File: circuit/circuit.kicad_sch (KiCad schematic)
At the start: 3 parts, among them J1 USB_B_Mini, U1 ESP-C3-WROOM-02, U2 nRF52820-QDAA

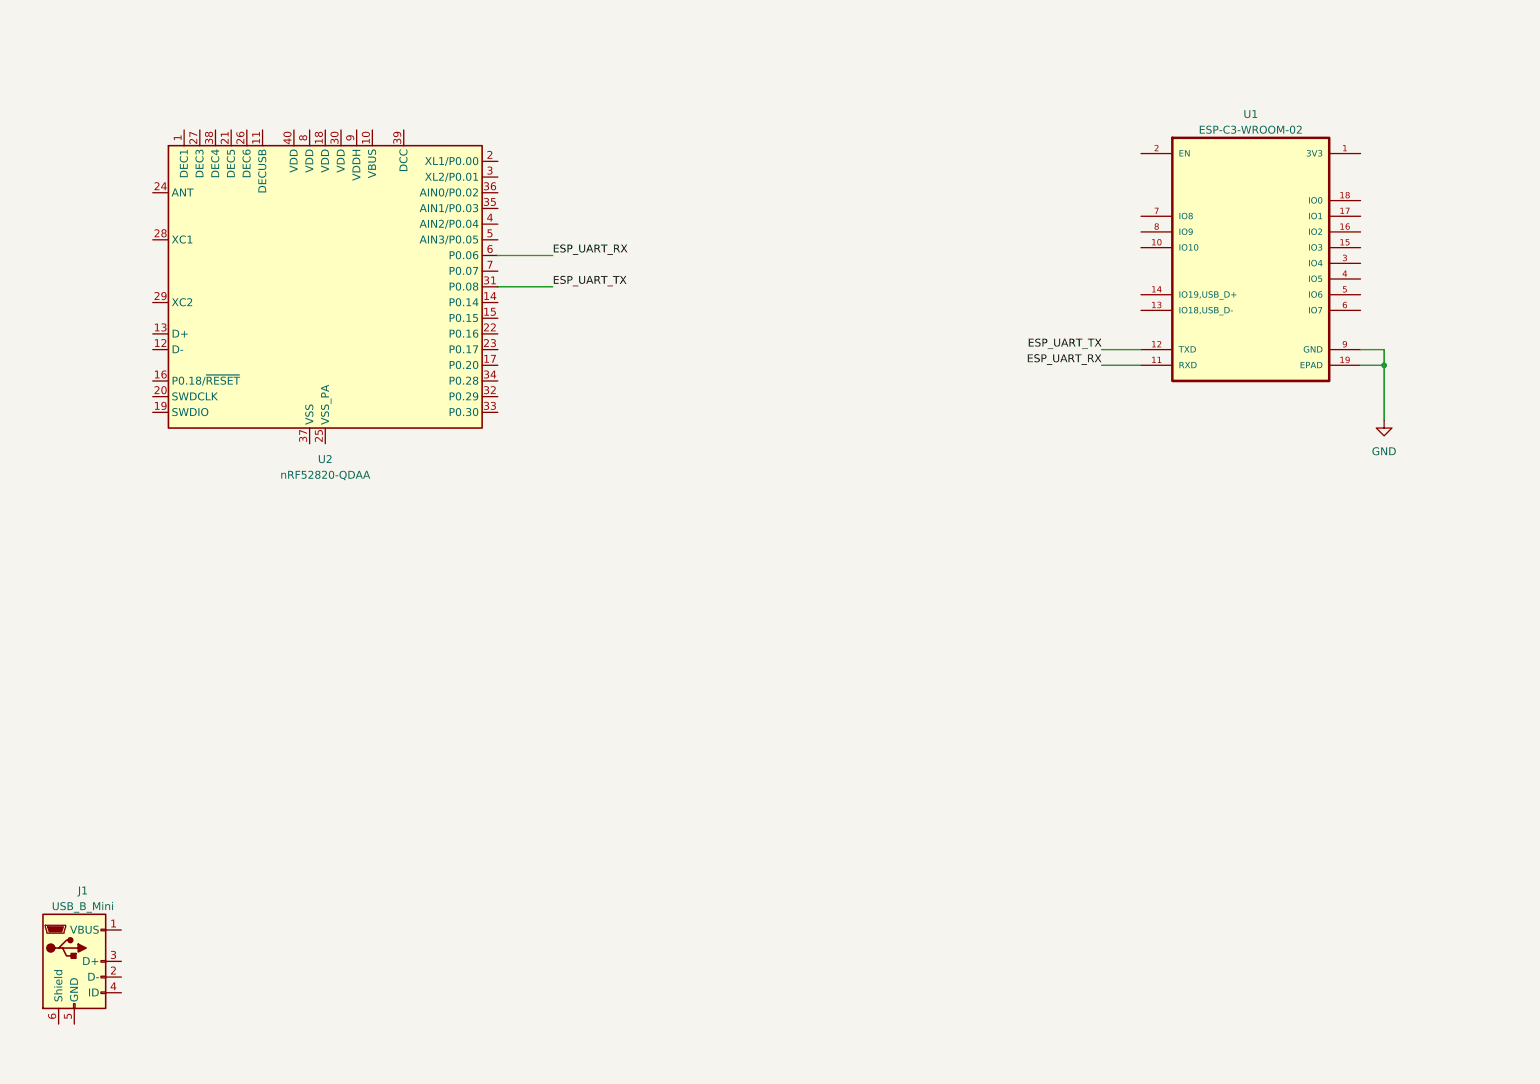
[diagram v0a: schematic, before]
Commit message: change(mdbt50): use module for 802.15.4
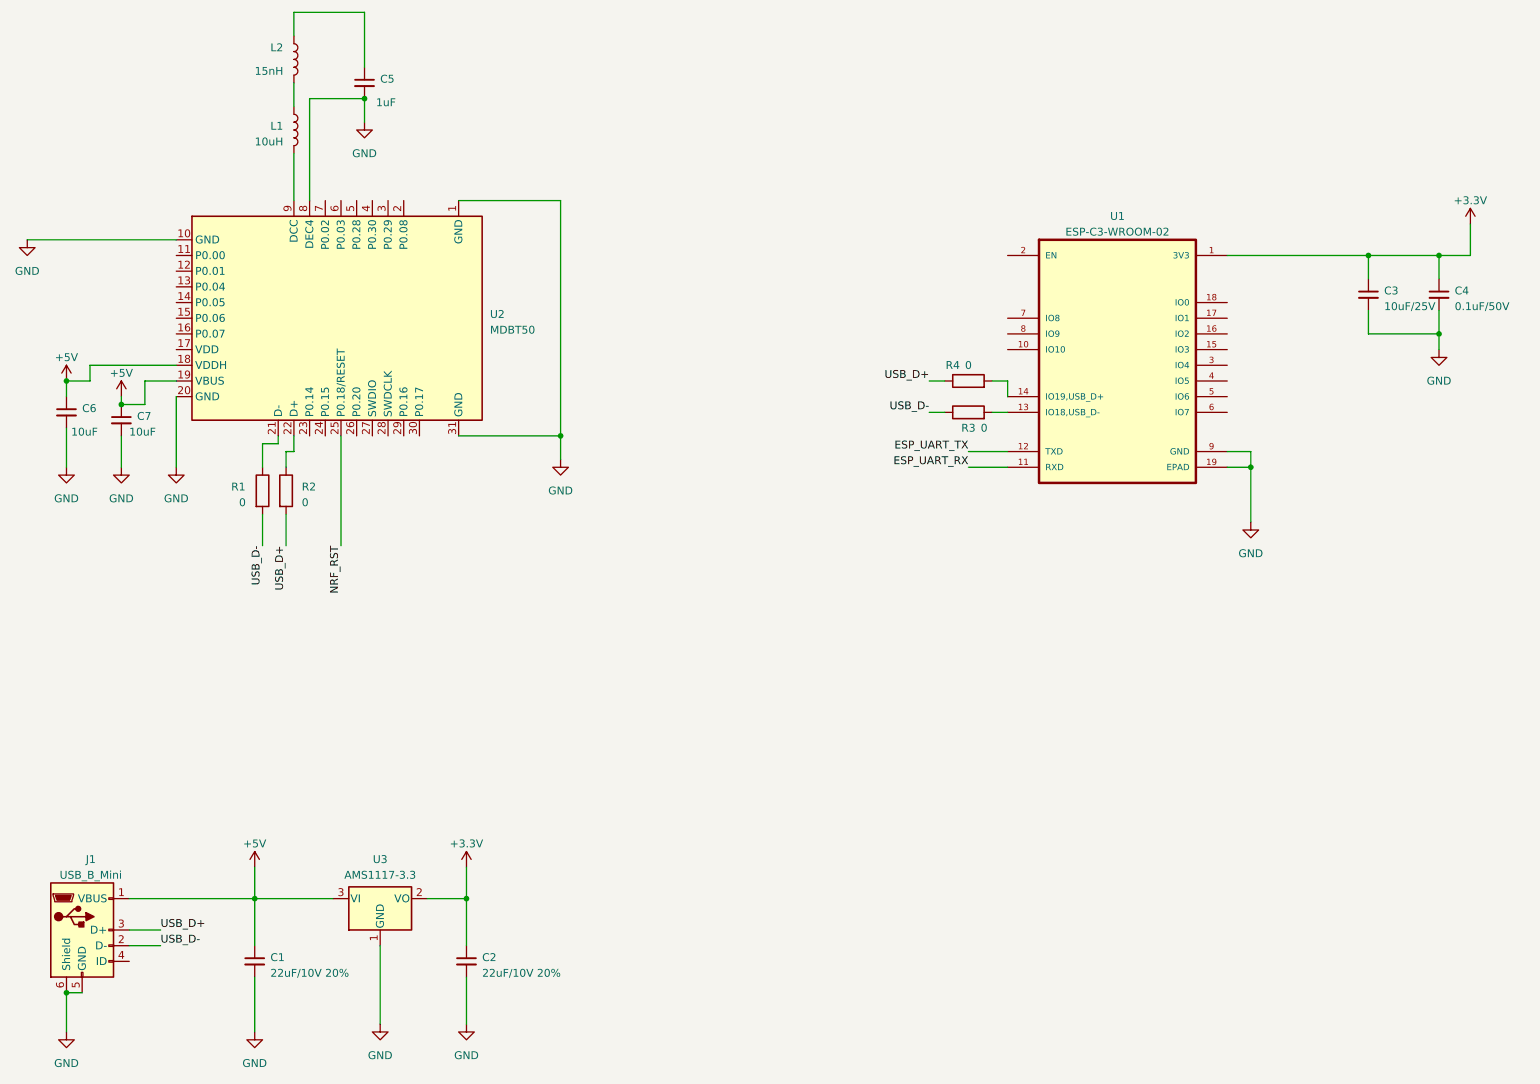
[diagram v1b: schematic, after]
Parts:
- removed U2: nRF52820-QDAA, Package_DFN_QFN:QFN-40-1EP_5x5mm_P0.4mm_EP3.6x3.6mm, symbol MCU_Nordic:nRF52820-QDxx
- added C1, C2: 22uF/10V 20%, Capacitor_SMD:C_0402_1005Metric, symbol Device:C_Small
- added C3: 10uF/25V, Capacitor_SMD:C_0402_1005Metric, symbol Device:C_Small
- added C4: 0.1uF/50V, Capacitor_SMD:C_0402_1005Metric, symbol Device:C_Small
- added C5: 1uF, Capacitor_SMD:C_0402_1005Metric, symbol Device:C_Small
- added C6, C7: 10uF, Capacitor_SMD:C_0402_1005Metric, symbol Device:C_Small
- added L1: 10uH, Inductor_SMD:L_0603_1608Metric, symbol Device:L
- added L2: 15nH, Inductor_SMD:L_0603_1608Metric, symbol Device:L
- added R1, R2, R3, R4: 0, Resistor_SMD:R_0603_1608Metric, symbol Device:R
- added U2: MDBT50, Module:MDBT50, symbol module_raytec:MDBT50
- added U3: AMS1117-3.3, Package_TO_SOT_SMD:SOT-223-3_TabPin2, symbol Regulator_Linear:AMS1117-3.3
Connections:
- net GND: now also J1.5 (GND), J1.6 (Shield), C1.2, C2.2, C3.2, C4.2, C5.2, C6.2, C7.2, U2.1 (GND), U2.10 (GND), U2.20 (GND), U2.31 (GND), U2.8 (DEC4), U3.1 (GND)
- net +3V3: now reaches U1.1 (3V3)
- net +3V3: now also C2.1, C3.1, C4.1, U3.2 (VO)
- net at U1.13 (IO18,USB_D-): now also R3.2
- net at U1.14 (IO19,USB_D+): now also R4.2
- net +5V: now reaches J1.1 (VBUS)
- net +5V: now also C1.1, C6.1, C7.1, U2.18 (VDDH), U2.19 (VBUS), U3.3 (VI)
- net USB_D-: now reaches J1.2 (D-)
- net USB_D-: now also R1.2, R3.1
- net USB_D+: now reaches J1.3 (D+)
- net USB_D+: now also R2.2, R4.1
- new net: C5.1, L2.1
- new net: L1.1, L2.2
- new net: R1.1, U2.21 (D-)
- new net: R2.1, U2.22 (D+)
- new net: L1.2, U2.9 (DCC)
- new net NRF_RST: U2.25 (P0.18/RESET)
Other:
- moved on the sheet: J1, U1
